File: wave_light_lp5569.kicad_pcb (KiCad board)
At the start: 2 copper layers, 53.1 x 60.7 mm, 25 parts, among them J1 Conn_01x06_Male, J10 Conn_01x02_Male, J11 Conn_01x02_Male, J12 Conn_01x02_Male, J13 Conn_01x02_Male, J14 Conn_01x02_Male, J2 Conn_02x04_Odd_Even, J3 Conn_01x06_Female, J4 Conn_01x03_Male, J5 Conn_01x02_Male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

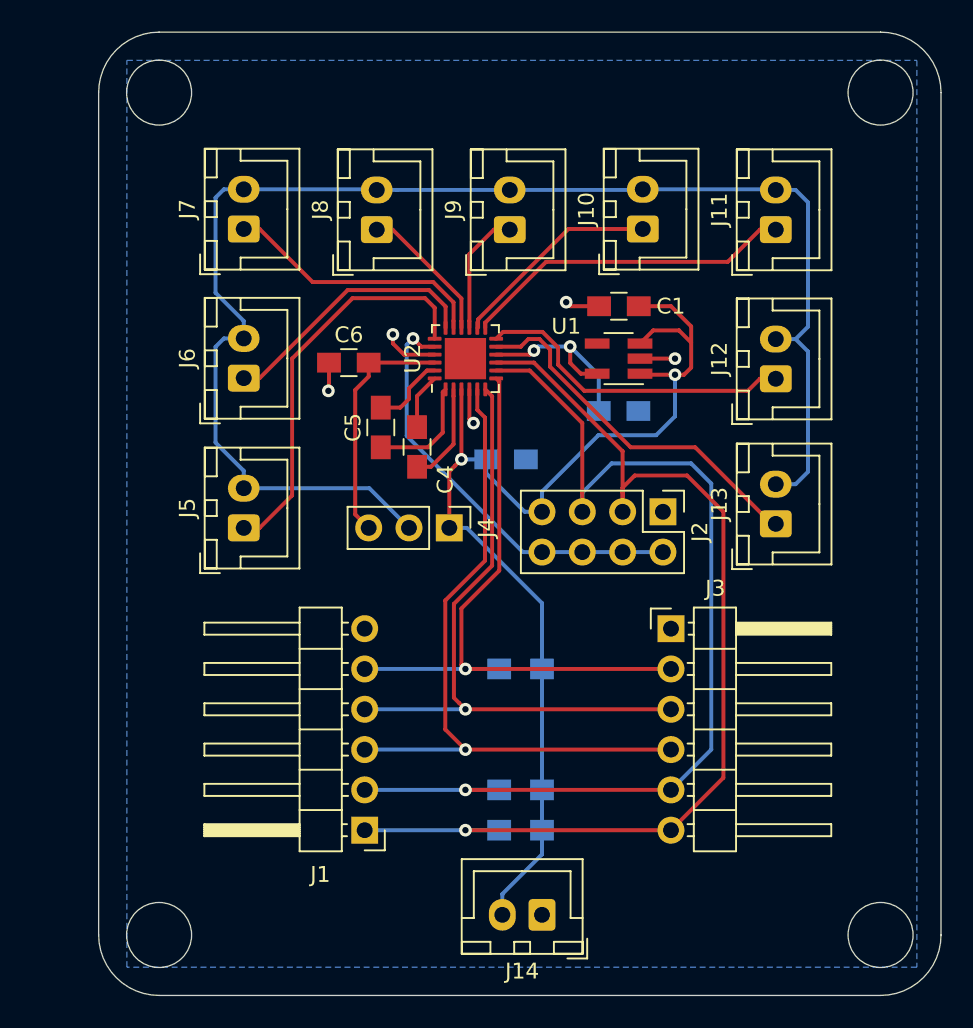
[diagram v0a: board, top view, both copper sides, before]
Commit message: First go at a wedge-shaped board
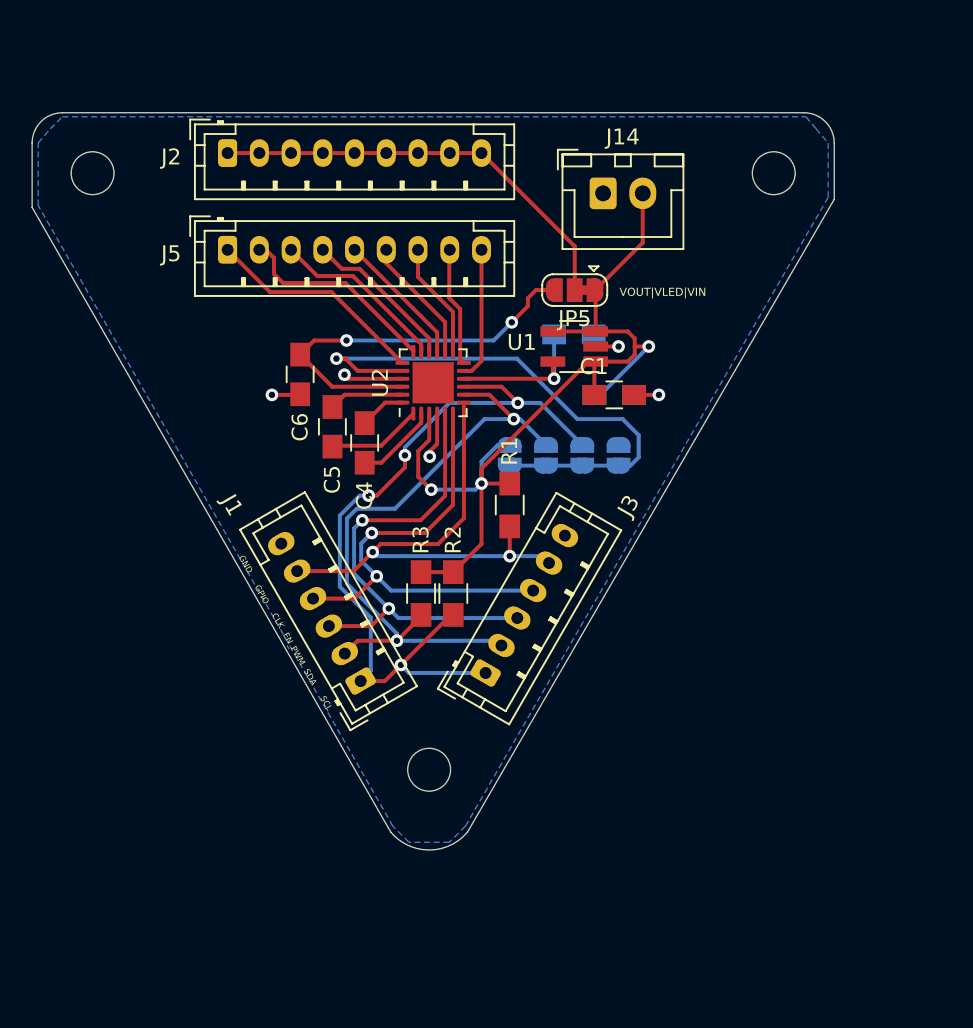
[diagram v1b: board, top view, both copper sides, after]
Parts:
- removed J10, J11, J12, J13, J6, J7, J8, J9: Conn_01x02_Male, Connector_JST:JST_XH_B2B-XH-A_1x02_P2.50mm_Vertical
- removed J4: Conn_01x03_Male, Pin_Headers:Pin_Header_Straight_1x03_Pitch2.54mm
- added H1: MountingHole, MountingHole:MountingHole_2.7mm, F.Cu at (93.6, 80.0)
- added H2: MountingHole, MountingHole:MountingHole_2.7mm, F.Cu at (136.5, 80.0)
- added H3: MountingHole, MountingHole:MountingHole_2.7mm, F.Cu at (114.8, 117.6)
- added JP1: SolderJumper_2_Open, Jumper:SolderJumper-2_P1.3mm_Open_RoundedPad1.0x1.5mm, B.Cu at (126.7, 97.8)
- added JP2: SolderJumper_2_Open, Jumper:SolderJumper-2_P1.3mm_Open_RoundedPad1.0x1.5mm, B.Cu at (124.5, 97.8)
- added JP3: SolderJumper_2_Open, Jumper:SolderJumper-2_P1.3mm_Open_RoundedPad1.0x1.5mm, B.Cu at (122.2, 97.8)
- added JP4: SolderJumper_2_Open, Jumper:SolderJumper-2_P1.3mm_Open_RoundedPad1.0x1.5mm, B.Cu at (119.9, 97.8)
- added JP5: SolderJumper_3_Bridged12, Jumper:SolderJumper-3_P1.3mm_Bridged12_RoundedPad1.0x1.5mm, F.Cu at (124.0, 87.4)
- J1: footprint Pin_Headers:Pin_Header_Angled_1x06_Pitch2.54mm -> Connector_JST:JST_PH_B6B-PH-K_1x06_P2.00mm_Vertical
- J2: value Conn_02x04_Odd_Even -> Conn_01x09_Male; footprint Pin_Headers:Pin_Header_Straight_2x04_Pitch2.54mm -> Connector_JST:JST_PH_B9B-PH-K_1x09_P2.00mm_Vertical
- J3: value Conn_01x06_Female -> Conn_01x06_Male; footprint Pin_Headers:Pin_Header_Angled_1x06_Pitch2.54mm -> Connector_JST:JST_PH_B6B-PH-K_1x06_P2.00mm_Vertical
- J5: value Conn_01x02_Male -> Conn_01x09_Male; footprint Connector_JST:JST_XH_B2B-XH-A_1x02_P2.50mm_Vertical -> Connector_JST:JST_PH_B9B-PH-K_1x09_P2.00mm_Vertical
- R1, R2, R3: moved to F.Cu
- moved J14 45.6 mm to (125.8, 81.3), turned to 0 degrees
- moved J2 35.5 mm to (102.1, 78.7), turned to 0 degrees
- moved J5 17.6 mm to (102.1, 84.8), turned to 0 degrees
- moved R2 15.5 mm to (116.3, 106.5), turned to 270 degrees
- moved R3 13.9 mm to (114.3, 106.5), turned to 270 degrees
- moved J3 12.0 mm to (118.4, 111.5), turned to 60 degrees
- moved R1 10.4 mm to (119.9, 100.9), turned to 270 degrees
- moved J1 9.40 mm to (110.5, 112.0), turned to 120 degrees
- moved C3 7.94 mm to (126.5, 94.0)
- moved C1 5.60 mm to (126.5, 94.0), turned to 180 degrees
- moved C2 5.59 mm to (123.9, 90.2)
- moved C4 3.31 mm to (110.7, 97.0)
- moved C6 3.16 mm to (106.7, 92.7), turned to 90 degrees
- moved C5 3.05 mm to (108.7, 96.0)
- moved U1 2.90 mm to (124.0, 90.9)
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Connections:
- J2 pad 1: GND -> VLED
- J2 pad 2: ADDR -> VLED
- J2 pad 3: SCL -> VLED
- J2 pad 4: ADDR -> VLED
- J2 pad 5: SDA -> VLED
- J2 pad 6: ADDR -> VLED
- J2 pad 7: VIN -> VLED
- J2 pad 8: ADDR -> VLED
- J3 pad 1: GND -> SCL
- J3 pad 2: GPIO_TRIG_INT -> SDA
- J3 pad 3: CLK -> EN_PWM
- J3 pad 4: EN_PWM -> CLK
- J3 pad 5: SDA -> GPIO_TRIG_INT
- J3 pad 6: SCL -> GND
- J5 pad 2: VLED -> LED1
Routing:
- net VLED: track 91.9 -> 27.1 mm
- net SDA: track 64.8 -> 41.3 mm, vias 1 -> 2
- net SCL: track 66.1 -> 48.5 mm, vias 1 -> 4
- net LED8: track 23.3 -> 8.38 mm
- net LED6: track 21.1 -> 7.36 mm
- net EN_PWM: track 43.8 -> 30.3 mm, vias 1 -> 2
- net VIN: track 72.5 -> 59.4 mm, vias 2 -> 3
- net LED7: track 20.3 -> 7.53 mm
- net LED0: track 25.3 -> 14.0 mm
- net CLK: track 40.9 -> 29.9 mm, vias 1 -> 2
- net VOUT: track 15.3 -> 25.3 mm, vias 0 -> 2
- net ADDR: track 27.1 -> 35.3 mm
- net GPIO_TRIG_INT: track 40.9 -> 33.1 mm, vias 1 -> 2
- net LED2: track 16.7 -> 11.2 mm
- net LED5: track 13.3 -> 7.98 mm
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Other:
- board size 53.1 x 60.7 mm -> 50.5 x 46.5 mm
- board text added: "32h"
- board text added: "33h"
- board text added: "34h"
- board text added: "35h"
- board text added: "Add 10h for LP5569A"
- board text added: "Address"
- board text added: "CLK"
- board text added: "EN_PWM"
- board text added: "GND"
- board text added: "GPIO"
- board text added: "SCL"
- board text added: "SDA"
- board text added: "VOUT|VLED|VIN"

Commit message: Checkpointing work on the wedge board
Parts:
- H1, H2, H3: footprint MountingHole:MountingHole_2.7mm -> MountingHole:MountingHole_2.7mm_Pad
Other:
- board text added: "+"
- board text added: "-"
- board text added: "5V MAX"
- board text added: "LED Control Board for Wave Light Wave Light by Roger Carr Board design by Robert Liesenfeld 2020 CC BY-SA 4.0 xunil@xunil.net"
- board text added: "LED GND"
- board text added: "VLED"

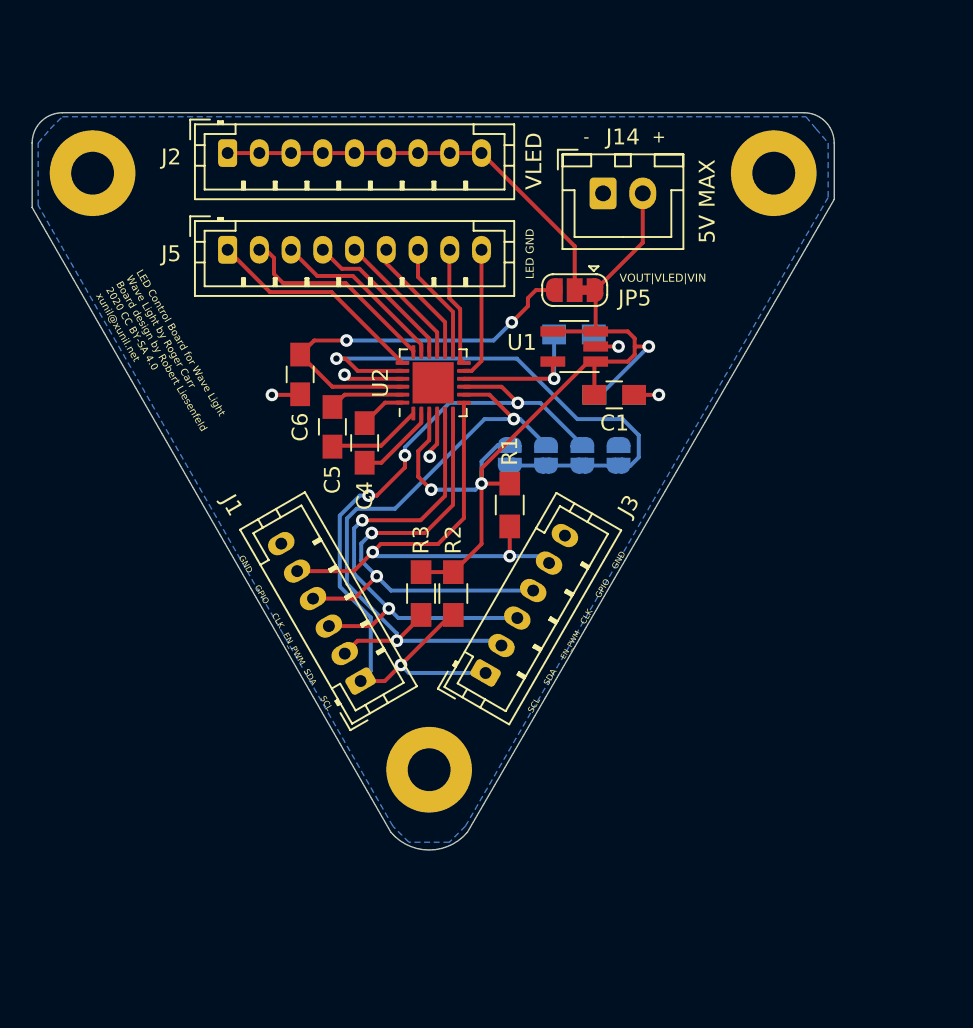
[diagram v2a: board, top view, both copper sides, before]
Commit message: Finally passing ERC and DRC, seems ready to send off for fab
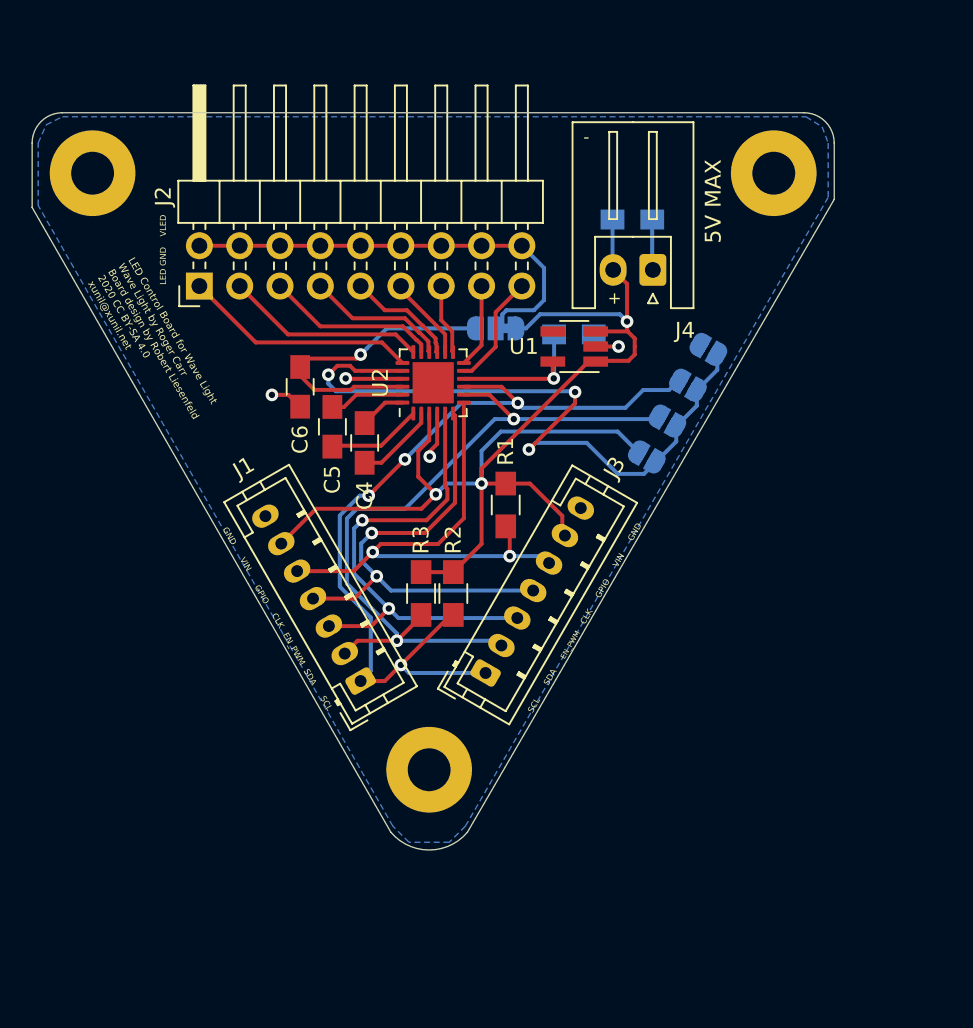
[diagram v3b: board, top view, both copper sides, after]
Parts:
- removed C3: 1uF, Capacitors_SMD:C_0805_HandSoldering
- removed J14: Conn_01x02_Male, Connector_JST:JST_XH_B2B-XH-A_1x02_P2.50mm_Vertical
- removed J5: Conn_01x09_Male, Connector_JST:JST_PH_B9B-PH-K_1x09_P2.00mm_Vertical
- added J4: Conn_01x02_Male, Connector_JST:JST_XH_S2B-XH-A_1x02_P2.50mm_Horizontal, F.Cu at (128.9, 86.1)
- C1, JP5: moved to B.Cu
- H1, H2: value MountingHole -> MountingHole_Pad
- H3: value MountingHole -> MountingHole_pad
- J1, J3: value Conn_01x06_Male -> Conn_01x07_Male; footprint Connector_JST:JST_PH_B6B-PH-K_1x06_P2.00mm_Vertical -> Connector_JST:JST_PH_B7B-PH-K_1x07_P2.00mm_Vertical
- J2: value Conn_01x09_Male -> Conn_02x09_Odd_Even; footprint Connector_JST:JST_PH_B9B-PH-K_1x09_P2.00mm_Vertical -> Connector_PinHeader_2.54mm:PinHeader_2x09_P2.54mm_Horizontal
- moved C1 11.1 mm to (127.6, 82.9)
- moved JP1 8.75 mm to (132.4, 91.1), turned to 330 degrees
- moved JP4 8.64 mm to (128.5, 97.9), turned to 330 degrees
- moved J2 8.57 mm to (100.3, 87.1), turned to 90 degrees
- moved JP2 7.99 mm to (131.1, 93.4), turned to 330 degrees
- moved JP3 7.94 mm to (129.8, 95.6), turned to 330 degrees
- moved JP5 5.54 mm to (119.0, 89.8)
- moved C6 0.78 mm to (106.7, 93.5)
- moved R1 0.25 mm to (119.6, 100.9)
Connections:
- H1 pad 1: (no net) -> GND
- H2 pad 1: (no net) -> GND
- H3 pad 1: (no net) -> GND
- J1 pad 6: GND -> VIN
- J2 pad 1: VLED -> LED0
- J2 pad 3: VLED -> LED1
- J2 pad 5: VLED -> LED2
- J2 pad 7: VLED -> LED3
- J2 pad 9: VLED -> LED4
- J3 pad 6: GND -> VIN
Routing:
- net VIN: track 59.4 -> 81.5 mm
- net ADDR: track 35.3 -> 43.9 mm, vias 1 -> 3
- net SDA: track 41.3 -> 47.8 mm
- net VOUT: track 25.3 -> 19.5 mm, vias 2 -> 1
- net SCL: track 48.5 -> 53.6 mm
- net LED6: track 7.36 -> 4.47 mm
- net LED5: track 7.98 -> 5.31 mm
- net LED7: track 7.53 -> 5.31 mm
- net GND: track 11.5 -> 13.5 mm, vias 5 -> 4
- net LED4: track 8.60 -> 7.02 mm
- net VLED: track 27.1 -> 28.6 mm
- net LED8: track 8.38 -> 7.14 mm
- net LED3: track 9.87 -> 8.95 mm
- net LED0: track 14.0 -> 14.8 mm
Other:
- board text added: "VIN"
- board text added: "VIN|VLED|VOUT"
- board text removed: "VOUT|VLED|VIN"

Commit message: Final version, sent to fab
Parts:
- added R4: 120k, Resistor_SMD:R_0805_2012Metric, B.Cu at (116.3, 105.7)
- C1, C2, C4, C5, C6: footprint Capacitors_SMD:C_0805_HandSoldering -> Capacitor_SMD:C_0805_2012Metric
- R1, R2, R3: footprint Resistors_SMD:R_0805_HandSoldering -> Resistor_SMD:R_0805_2012Metric
- U1: footprint TO_SOT_Packages_SMD:SOT-23-5_HandSoldering -> Package_TO_SOT_SMD:SOT-23-5
- moved R1 0.38 mm to (119.8, 100.6)
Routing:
- net VIN: track 81.5 -> 86.4 mm
- net GPIO_TRIG_INT: track 33.1 -> 29.5 mm
- net SCL: vias 4 -> 2
